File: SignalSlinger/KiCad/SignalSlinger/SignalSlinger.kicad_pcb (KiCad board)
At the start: 2 copper layers, 92.1 x 59.1 mm, 102 parts, among them J101 Conn_01x02, J103 Conn_01x02, J104 Conn_01x02, J105 Conn_01x02, J106 Conn_01x02, J107 DB9 Female, J108 Conn_01x02, J109 Conn_01x03, J112 External Power Source, J113 Controlled Power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

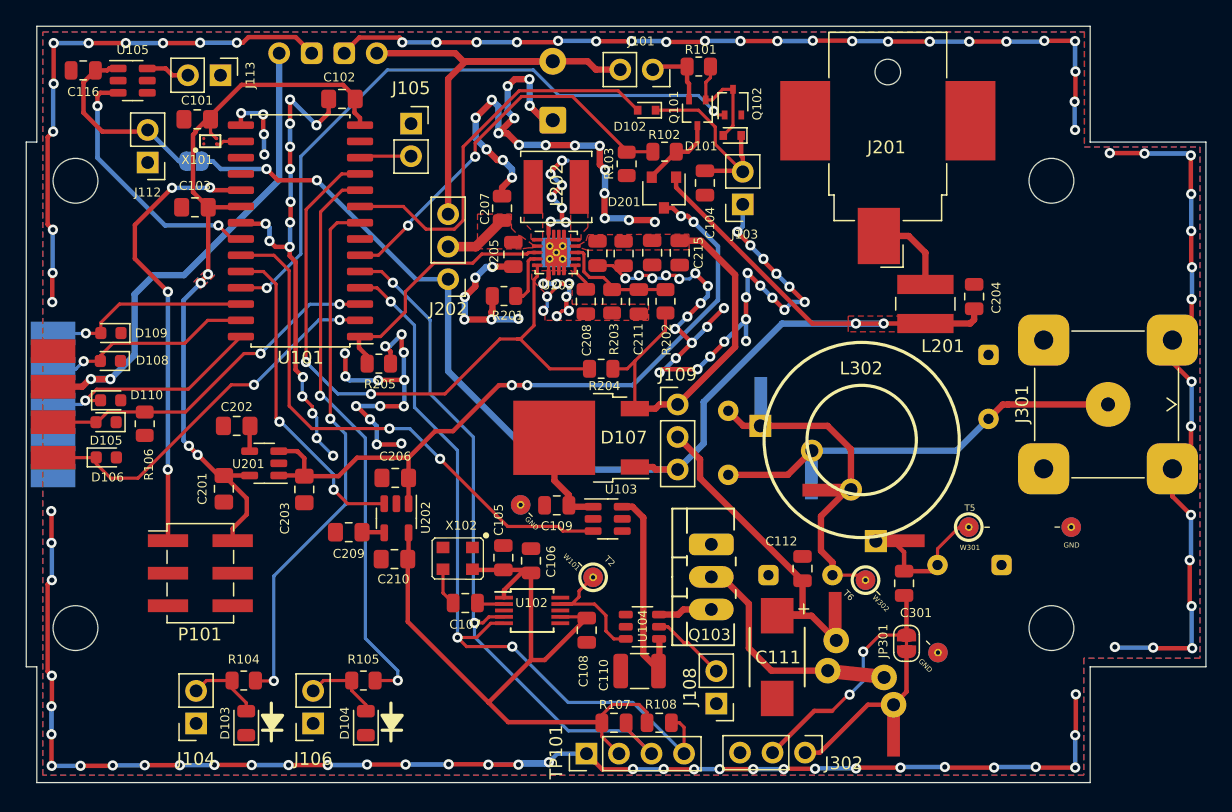
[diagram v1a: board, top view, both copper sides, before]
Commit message: PCB Development
Added stitching vias
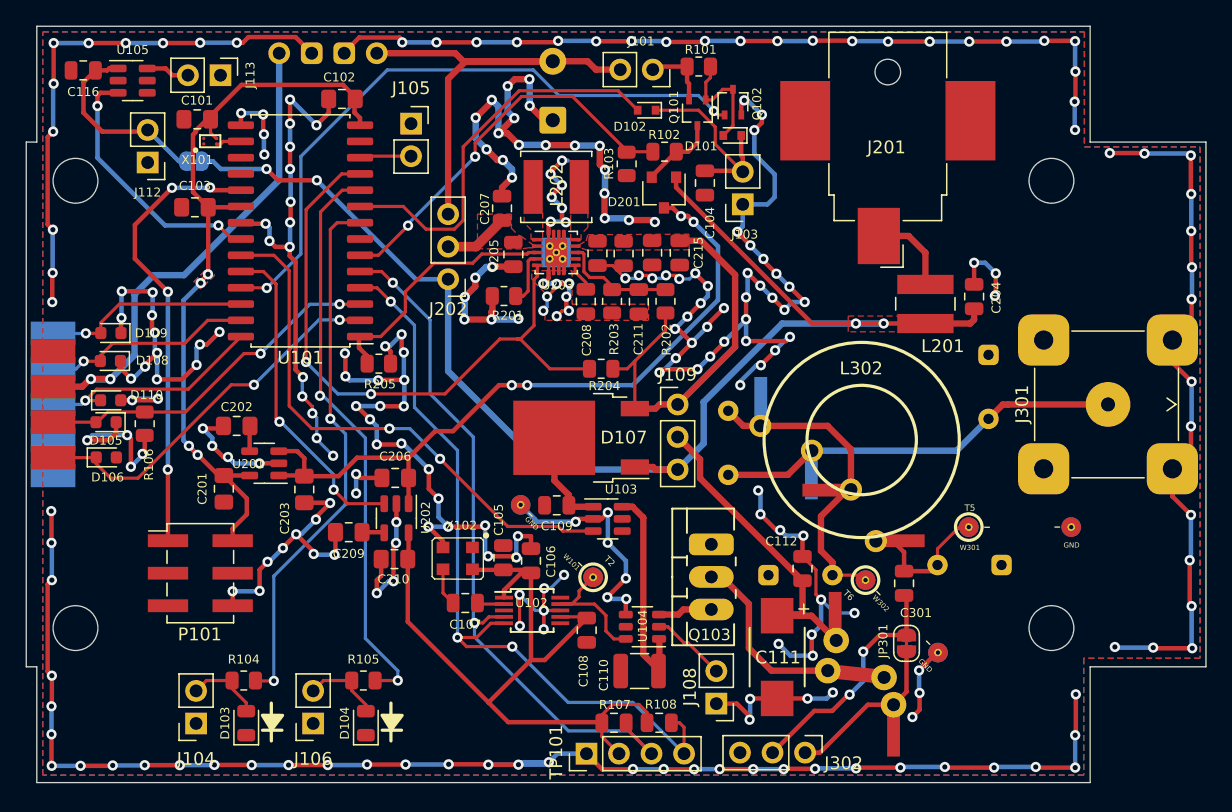
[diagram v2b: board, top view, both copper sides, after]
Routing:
- net GND: track 468.8 -> 676.3 mm, vias 187 -> 270

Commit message: Development
o Added polarity protection diode
o Tweaks to PCB
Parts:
- added D202: D_Schottky_Filled, Diode_SMD:D_SMA, F.Cu at (112.1, 80.9)
- C111: value 47 uF low ESR -> 47uF low ESR
- L201: value choke -> 2.2uH
- moved BT201 4.51 mm to (89.3, 62.7), turned to -90 degrees
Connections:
- BT201 pad 1: GND -> +BATT
- BT201 pad 2: +BATT -> GND
- L201 pad 1: Net-(J201-Pad1) -> Net-(L201-Pad1)
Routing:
- net GND: track 676.3 -> 684.7 mm, vias 270 -> 274
- net Net-(L201-Pad1): track 0.00 -> 4.42 mm
- net Net-(J201-Pad1): track 6.66 -> 8.39 mm
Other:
- board text added: "+"
- board text added: "-"

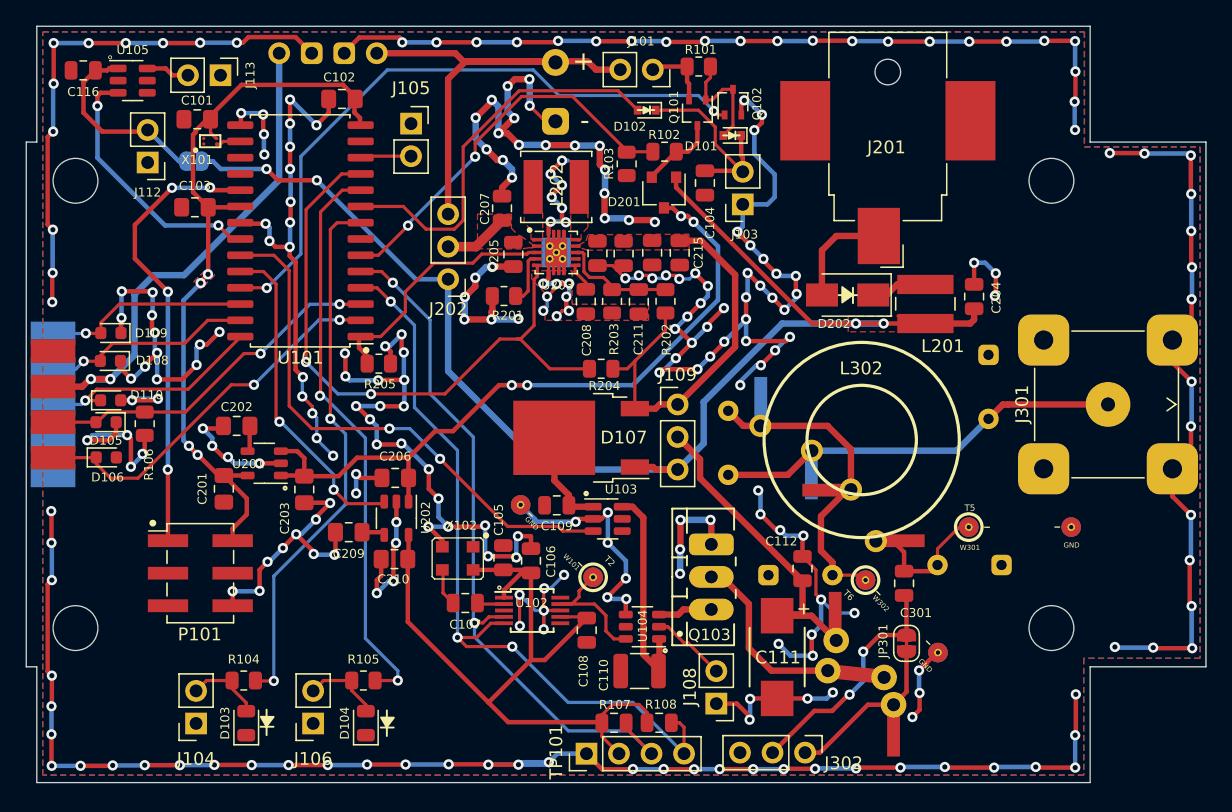
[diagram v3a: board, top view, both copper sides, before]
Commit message: PCB Development
Silkscreen updates
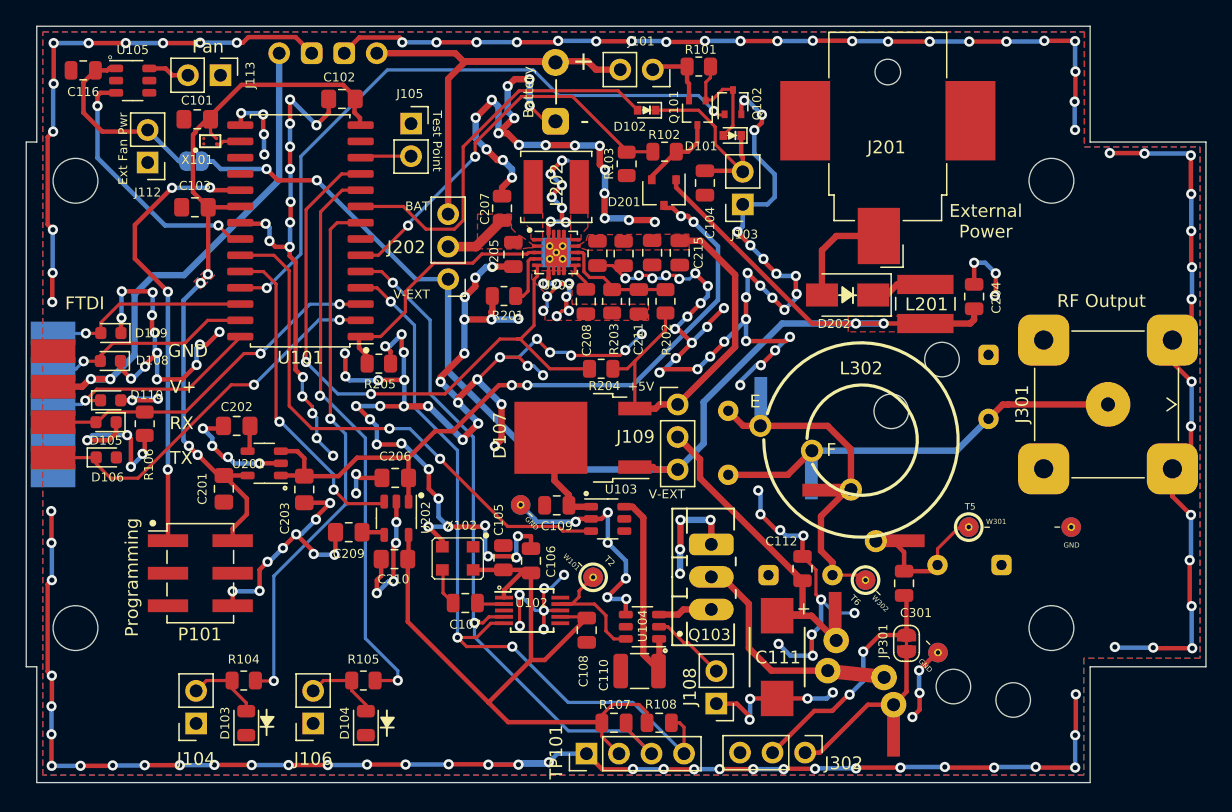
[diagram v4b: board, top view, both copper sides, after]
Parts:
- added REF**: MountingHole_2.7mm, MountingHole:MountingHole_2.7mm, F.Cu at (115.5, 90.0)
- added REF**: MountingHole_2.7mm, MountingHole:MountingHole_2.7mm, F.Cu at (125.1, 112.5)
- added REF**: MountingHole_2.7mm, MountingHole:MountingHole_2.7mm, F.Cu at (119.5, 85.9)
- added REF**: MountingHole_2.7mm, MountingHole:MountingHole_2.7mm, F.Cu at (120.4, 111.4)
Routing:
- net GND: track 684.7 -> 723.0 mm, vias 274 -> 291
- net Net-(C301-Pad2): track 11.3 -> 9.91 mm
- net VDD: track 61.0 -> 59.9 mm
- net Net-(L101-Pad2): track 14.1 -> 13.3 mm
- net Net-(C303-Pad2): track 24.9 -> 24.1 mm
- net +3V3: track 60.0 -> 59.2 mm
- net Fan_Contr: track 20.4 -> 19.7 mm
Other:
- board text added: "+5V"
- board text added: "Adafruit LiIon Charging Module PID_1904"
- board text added: "BAT"
- board text added: "Battery"
- board text added: "Battery Switch"
- board text added: "D"
- board text added: "DAH"
- board text added: "DIT"
- board text added: "Ext Fan Pwr"
- board text added: "External Power"
- board text added: "FTDI"
- board text added: "Fan"
- board text added: "Foxoring Module"
- board text added: "G"
- board text added: "GND"
- board text added: "Green LED"
- board text added: "I2C Test Point"
- board text added: "KEY"
- board text added: "PS Heat Sink"
- board text added: "Programming"
- board text added: "Pushbutton"
- board text added: "RF Output"
- board text added: "RX"
- board text added: "Red LED"
- board text added: "S"
- board text added: "SignalSlinger github.com/OpenARDF/SignalSlinger Open Source: MIT License Model: SS-80/40 June 2023"
- board text added: "TM"
- board text added: "TX"
- board text added: "Test Point"
- board text added: "V+"
- board text added: "V-EXT"
- board text removed: "SignalSlinger (TM) Model: SS-80/40 June 2023"

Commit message: Minor Edits
Schematic and PCB tweaks
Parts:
- J301: footprint Connector_Coaxial:BNC_TEConnectivity_1478035_Horizontal -> Connector_Coaxial:BNC_Amphenol_B6252HB-NPP3G-50_Horizontal
- moved J301 5.20 mm to (127.3, 89.4)
- moved C305 0.20 mm to (122.9, 90.5)
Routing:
- net GND: track 723.0 -> 740.4 mm, vias 291 -> 293
- net Net-(C304-Pad1): track 31.9 -> 26.8 mm
